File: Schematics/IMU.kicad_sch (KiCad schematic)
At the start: 0 parts

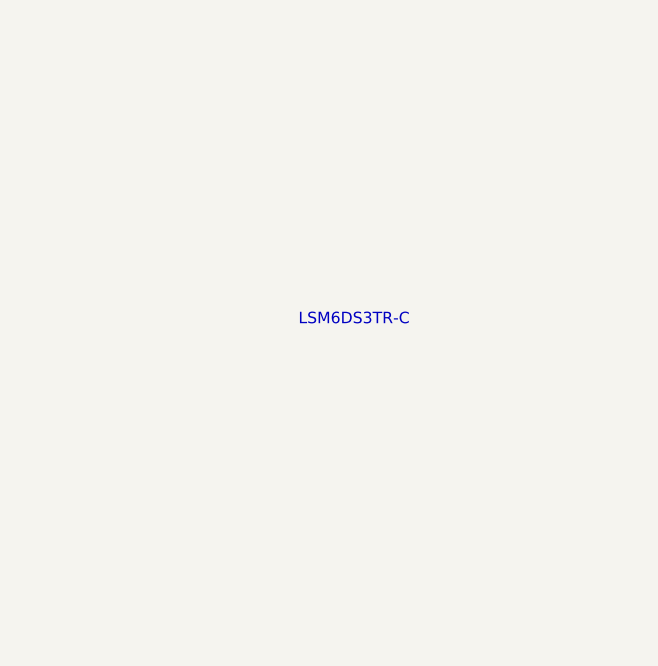
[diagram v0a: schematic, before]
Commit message: finished sensor schematics, added datasheets organized files
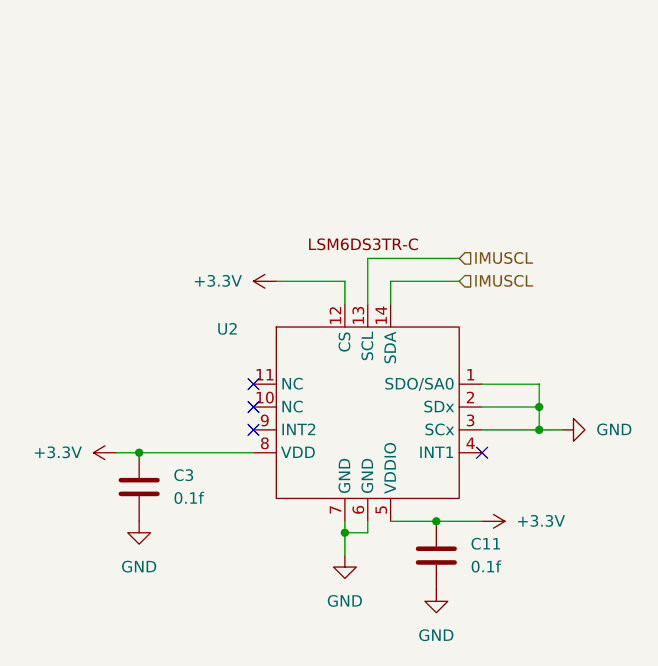
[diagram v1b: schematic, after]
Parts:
- added C11, C3: 0.1f, symbol Device:C
- added U2: ~, symbol Footprints:LSM6DS3TR-C
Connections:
- new net +3.3V: C11.1, C3.1, U2.12 (CS), U2.5 (VDDIO), U2.8 (VDD)
- new net GND: C11.2, C3.2, U2.1 (SDO/SA0), U2.2 (SDx), U2.3 (SCx), U2.6 (GND), U2.7 (GND)
- new net IMUSCL: U2.13 (SCL), U2.14 (SDA)
- no-connect marks 0 -> 4
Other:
- note removed: "LSM6DS3TR-C"

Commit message: added LCSC numbers and footprint values, need to connect schemeatic pins, then can start layout
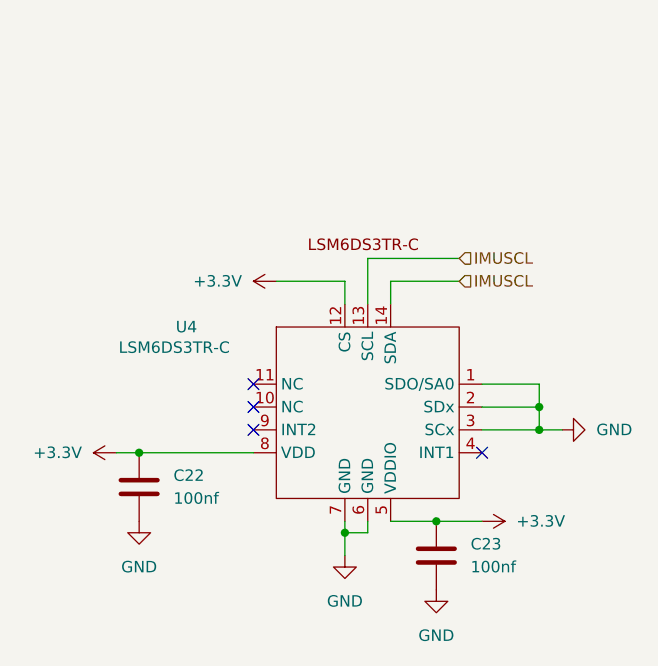
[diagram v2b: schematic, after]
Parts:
- C22: renamed from C3; value 0.1f -> 100nf; footprint (none) -> Capacitor_SMD:C_0805_2012Metric_Pad1.18x1.45mm_HandSolder; LCSC Part (none) -> C49678
- C23: renamed from C11; value 0.1f -> 100nf; footprint (none) -> Capacitor_SMD:C_0805_2012Metric_Pad1.18x1.45mm_HandSolder; LCSC Part (none) -> C49678
- U4: renamed from U2; value ~ -> LSM6DS3TR-C; footprint (none) -> myFootprints:LGA-14-2.5X3MM; LCSC Part (none) -> C967633
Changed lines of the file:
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@@
 		(dnp no)
 		(fields_autoplaced yes)
-		(property "Reference" "#PWR010"
+		(property "Reference" "#PWR067"
 			(at 118.11 106.68 0)
 			(effects
@@
 			(project ""
 				(path "/6cb3dda3-5fe8-4715-b831-354360aa3199/baf5f864-5fa3-4fb9-89f7-279135a67e52"
-					(reference "#PWR010")
+					(reference "#PWR067")
 					(unit 1)
 				)
@@
 		(dnp no)
 		(fields_autoplaced yes)
-		(property "Reference" "#PWR015"
+		(property "Reference" "#PWR072"
 			(at 151.13 114.3 0)
 			(effects
@@
 			(project ""
 				(path "/6cb3dda3-5fe8-4715-b831-354360aa3199/baf5f864-5fa3-4fb9-89f7-279135a67e52"
-					(reference "#PWR015")
+					(reference "#PWR072")
 					(unit 1)
 				)
@@
 		(dnp no)
 		(fields_autoplaced yes)
-		(property "Reference" "#PWR022"
+		(property "Reference" "#PWR069"
 			(at 135.89 87.63 0)
 			(effects
@@
 			(project "flightcomputer2"
 				(path "/6cb3dda3-5fe8-4715-b831-354360aa3199/baf5f864-5fa3-4fb9-89f7-279135a67e52"
-					(reference "#PWR022")
+					(reference "#PWR069")
 					(unit 1)
 				)
@@
 		(dnp no)
 		(fields_autoplaced yes)
-		(property "Reference" "#PWR016"
+		(property "Reference" "#PWR071"
 			(at 149.86 128.27 0)
 			(effects
@@
 			(project ""
 				(path "/6cb3dda3-5fe8-4715-b831-354360aa3199/baf5f864-5fa3-4fb9-89f7-279135a67e52"
-					(reference "#PWR016")
+					(reference "#PWR071")
 					(unit 1)
 				)
@@
 		(dnp no)
 		(fields_autoplaced yes)
-		(property "Reference" "#PWR011"
+		(property "Reference" "#PWR068"
 			(at 116.84 120.65 0)
 			(effects
@@
 			(project ""
 				(path "/6cb3dda3-5fe8-4715-b831-354360aa3199/baf5f864-5fa3-4fb9-89f7-279135a67e52"
-					(reference "#PWR011")
+					(reference "#PWR068")
 					(unit 1)
 				)
@@
 		(on_board yes)
 		(dnp no)
-		(property "Reference" "U2"
-			(at 125.476 92.964 0)
-			(effects
-				(font
-					(size 1.27 1.27)
-				)
-				(justify left)
-			)
-		)
-		(property "Value" "~"
-			(at 125.476 95.504 0)
-			(effects
-				(font
-					(size 1.27 1.27)
-				)
-				(justify left)
-			)
-		)
-		(property "Footprint" ""
+		(property "Reference" "U4"
+			(at 120.904 92.71 0)
+			(effects
+				(font
+					(size 1.27 1.27)
+				)
+				(justify left)
+			)
+		)
+		(property "Value" "LSM6DS3TR-C"
+			(at 114.554 94.996 0)
+			(effects
+				(font
+					(size 1.27 1.27)
+				)
+				(justify left)
+			)
+		)
+		(property "Footprint" "myFootprints:LGA-14-2.5X3MM"
 			(at 139.7 113.03 0)
 			(effects
@@
 			)
 		)
+		(property "LCSC Part" "C967633"
+			(at 139.7 113.03 0)
+			(effects
+				(font
+					(size 1.27 1.27)
+				)
+				(hide yes)
+			)
+		)
+		(property "Sim.Device" ""
+			(at 139.7 113.03 0)
+			(effects
+				(font
+					(size 1.27 1.27)
+				)
+				(hide yes)
+			)
+		)
+		(property "Sim.Type" ""
+			(at 139.7 113.03 0)
+			(effects
+				(font
+					(size 1.27 1.27)
+				)
+				(hide yes)
+			)
+		)
 		(pin "11"
 		)
@@
 			(project ""
 				(path "/6cb3dda3-5fe8-4715-b831-354360aa3199/baf5f864-5fa3-4fb9-89f7-279135a67e52"
-					(reference "U2")
+					(reference "U4")
 					(unit 1)
 				)
@@
 		(dnp no)
 		(fields_autoplaced yes)
-		(property "Reference" "C3"
+		(property "Reference" "C22"
 			(at 120.65 109.2199 0)
 			(effects
@@
 			)
 		)
-		(property "Value" "0.1f"
+		(property "Value" "100nf"
 			(at 120.65 111.7599 0)
 			(effects
@@
 			)
 		)
-		(property "Footprint" ""
+		(property "Footprint" "Capacitor_SMD:C_0805_2012Metric_Pad1.18x1.45mm_HandSolder"
 			(at 117.8052 114.3 0)
 			(effects
@@
 			)
 		)
+		(property "Sim.Device" ""
+			(at 116.84 110.49 0)
+			(effects
+				(font
+					(size 1.27 1.27)
+				)
+				(hide yes)
+			)
+		)
+		(property "Sim.Type" ""
+			(at 116.84 110.49 0)
+			(effects
+				(font
+					(size 1.27 1.27)
+				)
+				(hide yes)
+			)
+		)
+		(property "LCSC Part" "C49678"
+			(at 116.84 110.49 0)
+			(effects
+				(font
+					(size 1.27 1.27)
+				)
+				(hide yes)
+			)
+		)
 		(pin "2"
 		)
@@
 			(project ""
 				(path "/6cb3dda3-5fe8-4715-b831-354360aa3199/baf5f864-5fa3-4fb9-89f7-279135a67e52"
-					(reference "C3")
+					(reference "C22")
 					(unit 1)
 				)
@@
 		(dnp no)
 		(fields_autoplaced yes)
-		(property "Reference" "C11"
+		(property "Reference" "C23"
 			(at 153.67 116.8399 0)
 			(effects
@@
 			)
 		)
-		(property "Value" "0.1f"
+		(property "Value" "100nf"
 			(at 153.67 119.3799 0)
 			(effects
@@
 			)
 		)
-		(property "Footprint" ""
+		(property "Footprint" "Capacitor_SMD:C_0805_2012Metric_Pad1.18x1.45mm_HandSolder"
 			(at 150.8252 121.92 0)
 			(effects
@@
 			)
 		)
+		(property "Sim.Device" ""
+			(at 149.86 118.11 0)
+			(effects
+				(font
+					(size 1.27 1.27)
+				)
+				(hide yes)
+			)
+		)
+		(property "Sim.Type" ""
+			(at 149.86 118.11 0)
+			(effects
+				(font
+					(size 1.27 1.27)
+				)
+				(hide yes)
+			)
+		)
+		(property "LCSC Part" "C49678"
+			(at 149.86 118.11 0)
+			(effects
+				(font
+					(size 1.27 1.27)
+				)
+				(hide yes)
+			)
+		)
 		(pin "1"
 		)
@@
 			(project ""
 				(path "/6cb3dda3-5fe8-4715-b831-354360aa3199/baf5f864-5fa3-4fb9-89f7-279135a67e52"
-					(reference "C11")
+					(reference "C23")
 					(unit 1)
 				)
@@
 		(dnp no)
 		(fields_autoplaced yes)
-		(property "Reference" "#PWR09"
+		(property "Reference" "#PWR073"
 			(at 170.18 104.14 0)
 			(effects
@@
 			(project ""
 				(path "/6cb3dda3-5fe8-4715-b831-354360aa3199/baf5f864-5fa3-4fb9-89f7-279135a67e52"
-					(reference "#PWR09")
+					(reference "#PWR073")
 					(unit 1)
 				)
@@
 		(dnp no)
 		(fields_autoplaced yes)
-		(property "Reference" "#PWR021"
+		(property "Reference" "#PWR070"
 			(at 139.7 124.46 0)
 			(effects
@@
 			(project ""
 				(path "/6cb3dda3-5fe8-4715-b831-354360aa3199/baf5f864-5fa3-4fb9-89f7-279135a67e52"
-					(reference "#PWR021")
-					(unit 1)
-				)
+					(reference "#PWR070")
+					(unit 1)
+				)

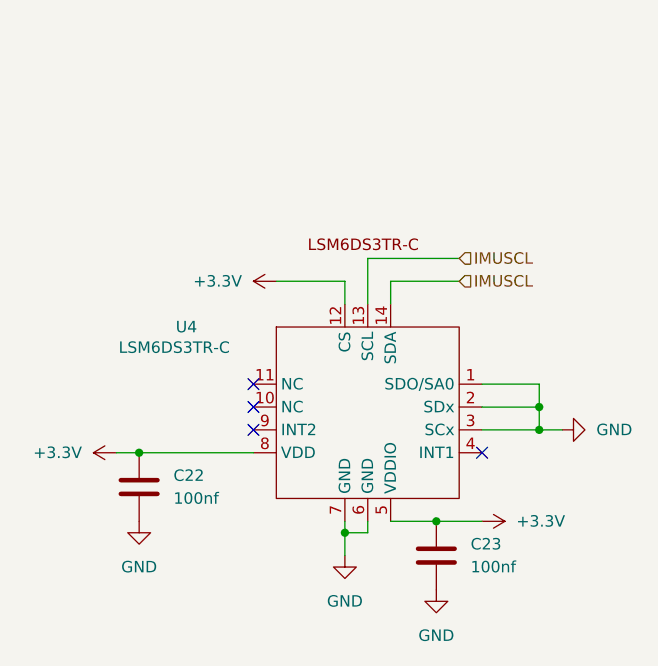
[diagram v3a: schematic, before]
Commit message: fixed symbols and added diodes to power input before ldo
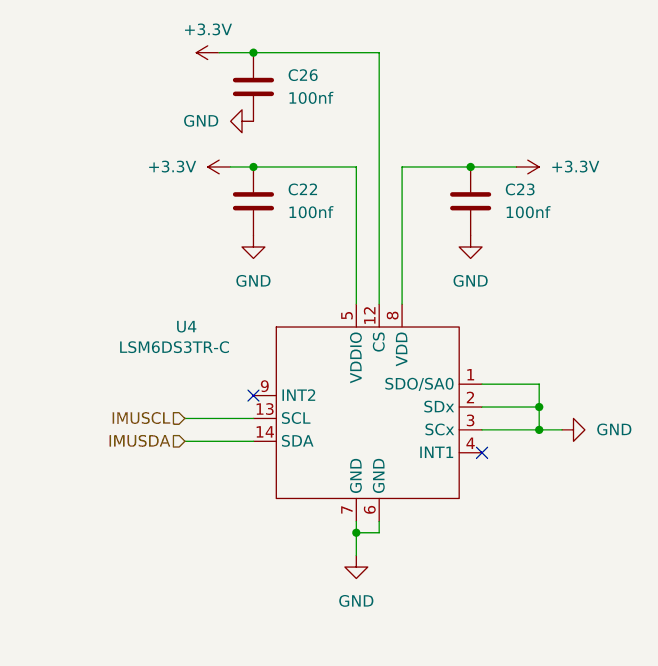
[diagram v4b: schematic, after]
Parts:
- added C26: 100nf, Capacitor_SMD:C_0805_2012Metric_Pad1.18x1.45mm_HandSolder, symbol Device:C
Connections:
- net +3.3V: now also C26.1
- net GND: now also C26.2
- net IMUSCL: no longer U4.14 (SDA)
- new net IMUSDA: U4.14 (SDA)
- no-connect marks 4 -> 2
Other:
- moved on the sheet: C22, C23

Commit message: added lora correct and organizing sheet pins
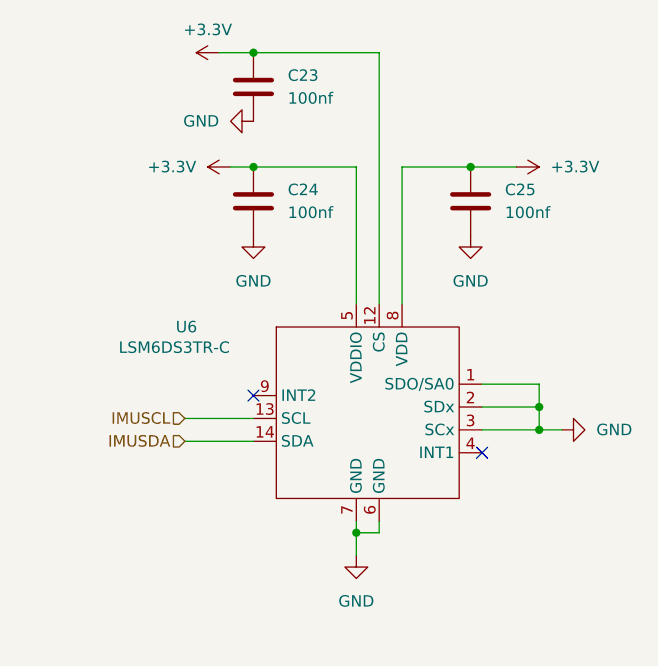
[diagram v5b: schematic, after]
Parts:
- renumbered C26 to C23, C22 to C24, C23 to C25, U4 to U6
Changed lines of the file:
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@@
 		(dnp no)
 		(fields_autoplaced yes)
-		(property "Reference" "#PWR067"
+		(property "Reference" "#PWR071"
 			(at 130.81 74.93 0)
 			(effects
@@
 			(project ""
 				(path "/6cb3dda3-5fe8-4715-b831-354360aa3199/baf5f864-5fa3-4fb9-89f7-279135a67e52"
-					(reference "#PWR067")
+					(reference "#PWR071")
 					(unit 1)
 				)
@@
 		(dnp no)
 		(fields_autoplaced yes)
-		(property "Reference" "#PWR072"
+		(property "Reference" "#PWR076"
 			(at 154.94 74.93 0)
 			(effects
@@
 			(project ""
 				(path "/6cb3dda3-5fe8-4715-b831-354360aa3199/baf5f864-5fa3-4fb9-89f7-279135a67e52"
-					(reference "#PWR072")
+					(reference "#PWR076")
 					(unit 1)
 				)
@@
 		(dnp no)
 		(fields_autoplaced yes)
-		(property "Reference" "#PWR069"
+		(property "Reference" "#PWR070"
 			(at 129.54 62.23 0)
 			(effects
@@
 			(project "flightcomputer2"
 				(path "/6cb3dda3-5fe8-4715-b831-354360aa3199/baf5f864-5fa3-4fb9-89f7-279135a67e52"
-					(reference "#PWR069")
+					(reference "#PWR070")
 					(unit 1)
 				)
@@
 		(dnp no)
 		(fields_autoplaced yes)
-		(property "Reference" "#PWR071"
+		(property "Reference" "#PWR075"
 			(at 153.67 88.9 0)
 			(effects
@@
 			(project ""
 				(path "/6cb3dda3-5fe8-4715-b831-354360aa3199/baf5f864-5fa3-4fb9-89f7-279135a67e52"
-					(reference "#PWR071")
+					(reference "#PWR075")
 					(unit 1)
 				)
@@
 		(dnp no)
 		(fields_autoplaced yes)
-		(property "Reference" "#PWR068"
+		(property "Reference" "#PWR073"
 			(at 129.54 88.9 0)
 			(effects
@@
 			(project ""
 				(path "/6cb3dda3-5fe8-4715-b831-354360aa3199/baf5f864-5fa3-4fb9-89f7-279135a67e52"
-					(reference "#PWR068")
+					(reference "#PWR073")
 					(unit 1)
 				)
@@
 		(dnp no)
 		(fields_autoplaced yes)
-		(property "Reference" "#PWR076"
+		(property "Reference" "#PWR072"
 			(at 123.19 69.85 0)
 			(effects
@@
 			(project "flightcomputer2"
 				(path "/6cb3dda3-5fe8-4715-b831-354360aa3199/baf5f864-5fa3-4fb9-89f7-279135a67e52"
-					(reference "#PWR076")
+					(reference "#PWR072")
 					(unit 1)
 				)
@@
 		(on_board yes)
 		(dnp no)
-		(property "Reference" "U4"
+		(property "Reference" "U6"
 			(at 120.904 92.71 0)
 			(effects
@@
 			(project ""
 				(path "/6cb3dda3-5fe8-4715-b831-354360aa3199/baf5f864-5fa3-4fb9-89f7-279135a67e52"
-					(reference "U4")
+					(reference "U6")
 					(unit 1)
 				)
@@
 		(dnp no)
 		(fields_autoplaced yes)
-		(property "Reference" "C26"
+		(property "Reference" "C23"
 			(at 133.35 64.7699 0)
 			(effects
@@
 			(project "flightcomputer2"
 				(path "/6cb3dda3-5fe8-4715-b831-354360aa3199/baf5f864-5fa3-4fb9-89f7-279135a67e52"
-					(reference "C26")
+					(reference "C23")
 					(unit 1)
 				)
@@
 		(dnp no)
 		(fields_autoplaced yes)
-		(property "Reference" "C22"
+		(property "Reference" "C24"
 			(at 133.35 77.4699 0)
 			(effects
@@
 			(project ""
 				(path "/6cb3dda3-5fe8-4715-b831-354360aa3199/baf5f864-5fa3-4fb9-89f7-279135a67e52"
-					(reference "C22")
+					(reference "C24")
 					(unit 1)
 				)
@@
 		(dnp no)
 		(fields_autoplaced yes)
-		(property "Reference" "C23"
+		(property "Reference" "C25"
 			(at 157.48 77.4699 0)
 			(effects
@@
 			(project ""
 				(path "/6cb3dda3-5fe8-4715-b831-354360aa3199/baf5f864-5fa3-4fb9-89f7-279135a67e52"
-					(reference "C23")
+					(reference "C25")
 					(unit 1)
 				)
@@
 		(dnp no)
 		(fields_autoplaced yes)
-		(property "Reference" "#PWR073"
+		(property "Reference" "#PWR077"
 			(at 170.18 104.14 0)
 			(effects
@@
 			(project ""
 				(path "/6cb3dda3-5fe8-4715-b831-354360aa3199/baf5f864-5fa3-4fb9-89f7-279135a67e52"
-					(reference "#PWR073")
+					(reference "#PWR077")
 					(unit 1)
 				)
@@
 		(dnp no)
 		(fields_autoplaced yes)
-		(property "Reference" "#PWR070"
+		(property "Reference" "#PWR074"
 			(at 140.97 124.46 0)
 			(effects
@@
 			(project ""
 				(path "/6cb3dda3-5fe8-4715-b831-354360aa3199/baf5f864-5fa3-4fb9-89f7-279135a67e52"
-					(reference "#PWR070")
-					(unit 1)
-				)
+					(reference "#PWR074")
+					(unit 1)
+				)

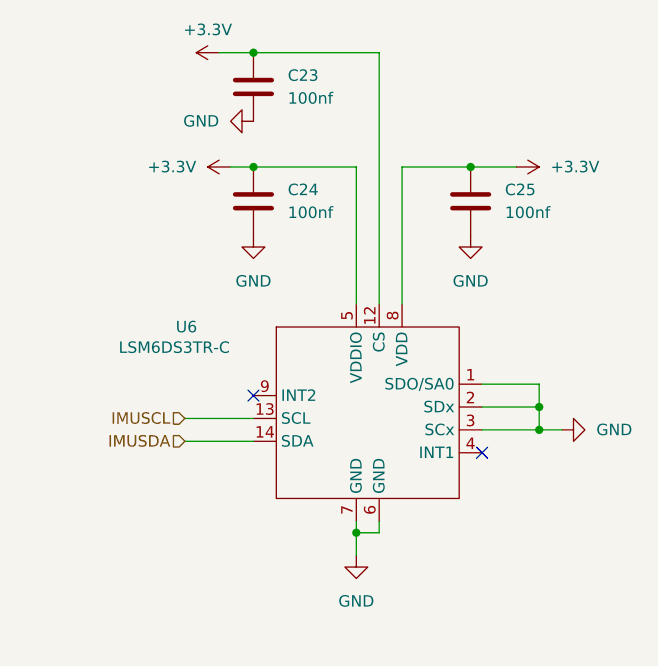
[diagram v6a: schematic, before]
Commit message: first layout need to go over schematic
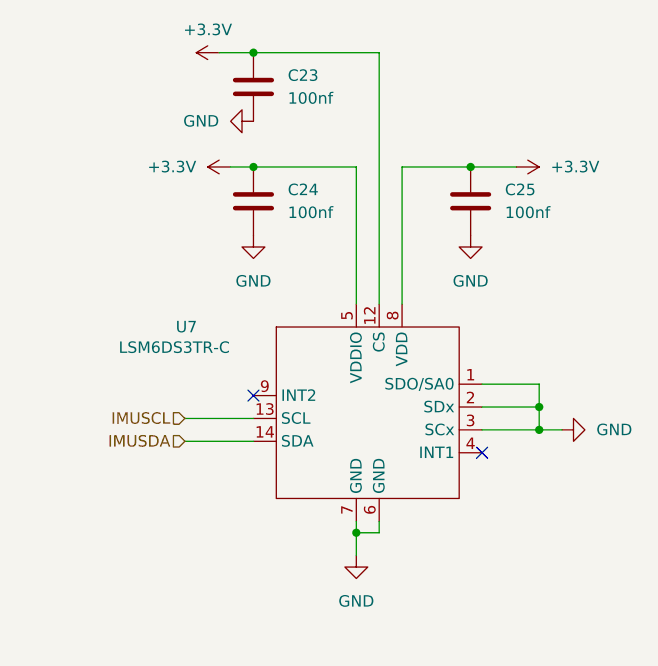
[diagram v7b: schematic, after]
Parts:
- renumbered U6 to U7
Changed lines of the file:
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@@
 		(dnp no)
 		(fields_autoplaced yes)
-		(property "Reference" "#PWR071"
+		(property "Reference" "#PWR077"
 			(at 130.81 74.93 0)
 			(effects
@@
 			(project ""
 				(path "/6cb3dda3-5fe8-4715-b831-354360aa3199/baf5f864-5fa3-4fb9-89f7-279135a67e52"
-					(reference "#PWR071")
+					(reference "#PWR077")
 					(unit 1)
 				)
@@
 		(dnp no)
 		(fields_autoplaced yes)
-		(property "Reference" "#PWR076"
+		(property "Reference" "#PWR082"
 			(at 154.94 74.93 0)
 			(effects
@@
 			(project ""
 				(path "/6cb3dda3-5fe8-4715-b831-354360aa3199/baf5f864-5fa3-4fb9-89f7-279135a67e52"
-					(reference "#PWR076")
+					(reference "#PWR082")
 					(unit 1)
 				)
@@
 		(dnp no)
 		(fields_autoplaced yes)
-		(property "Reference" "#PWR070"
+		(property "Reference" "#PWR076"
 			(at 129.54 62.23 0)
 			(effects
@@
 			(project "flightcomputer2"
 				(path "/6cb3dda3-5fe8-4715-b831-354360aa3199/baf5f864-5fa3-4fb9-89f7-279135a67e52"
-					(reference "#PWR070")
+					(reference "#PWR076")
 					(unit 1)
 				)
@@
 		(dnp no)
 		(fields_autoplaced yes)
-		(property "Reference" "#PWR075"
+		(property "Reference" "#PWR081"
 			(at 153.67 88.9 0)
 			(effects
@@
 			(project ""
 				(path "/6cb3dda3-5fe8-4715-b831-354360aa3199/baf5f864-5fa3-4fb9-89f7-279135a67e52"
-					(reference "#PWR075")
+					(reference "#PWR081")
 					(unit 1)
 				)
@@
 		(dnp no)
 		(fields_autoplaced yes)
-		(property "Reference" "#PWR073"
+		(property "Reference" "#PWR079"
 			(at 129.54 88.9 0)
 			(effects
@@
 			(project ""
 				(path "/6cb3dda3-5fe8-4715-b831-354360aa3199/baf5f864-5fa3-4fb9-89f7-279135a67e52"
-					(reference "#PWR073")
+					(reference "#PWR079")
 					(unit 1)
 				)
@@
 		(dnp no)
 		(fields_autoplaced yes)
-		(property "Reference" "#PWR072"
+		(property "Reference" "#PWR078"
 			(at 123.19 69.85 0)
 			(effects
@@
 			(project "flightcomputer2"
 				(path "/6cb3dda3-5fe8-4715-b831-354360aa3199/baf5f864-5fa3-4fb9-89f7-279135a67e52"
-					(reference "#PWR072")
+					(reference "#PWR078")
 					(unit 1)
 				)
@@
 		(on_board yes)
 		(dnp no)
-		(property "Reference" "U6"
+		(property "Reference" "U7"
 			(at 120.904 92.71 0)
 			(effects
@@
 			(project ""
 				(path "/6cb3dda3-5fe8-4715-b831-354360aa3199/baf5f864-5fa3-4fb9-89f7-279135a67e52"
-					(reference "U6")
+					(reference "U7")
 					(unit 1)
 				)
@@
 		(dnp no)
 		(fields_autoplaced yes)
-		(property "Reference" "#PWR077"
+		(property "Reference" "#PWR083"
 			(at 170.18 104.14 0)
 			(effects
@@
 			(project ""
 				(path "/6cb3dda3-5fe8-4715-b831-354360aa3199/baf5f864-5fa3-4fb9-89f7-279135a67e52"
-					(reference "#PWR077")
+					(reference "#PWR083")
 					(unit 1)
 				)
@@
 		(dnp no)
 		(fields_autoplaced yes)
-		(property "Reference" "#PWR074"
+		(property "Reference" "#PWR080"
 			(at 140.97 124.46 0)
 			(effects
@@
 			(project ""
 				(path "/6cb3dda3-5fe8-4715-b831-354360aa3199/baf5f864-5fa3-4fb9-89f7-279135a67e52"
-					(reference "#PWR074")
-					(unit 1)
-				)
+					(reference "#PWR080")
+					(unit 1)
+				)
